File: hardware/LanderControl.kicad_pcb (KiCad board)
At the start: 4 copper layers, 140 x 54 mm, 161 parts, among them J2 Conn_01x04, J3 Conn_01x05, J5 MEM2051-00-195-00-A, Q1 BC846, Q2 BC846, Q3 BC846, Q4 BC846, Q5 BC846, Q6 BC846, Q7 BC846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

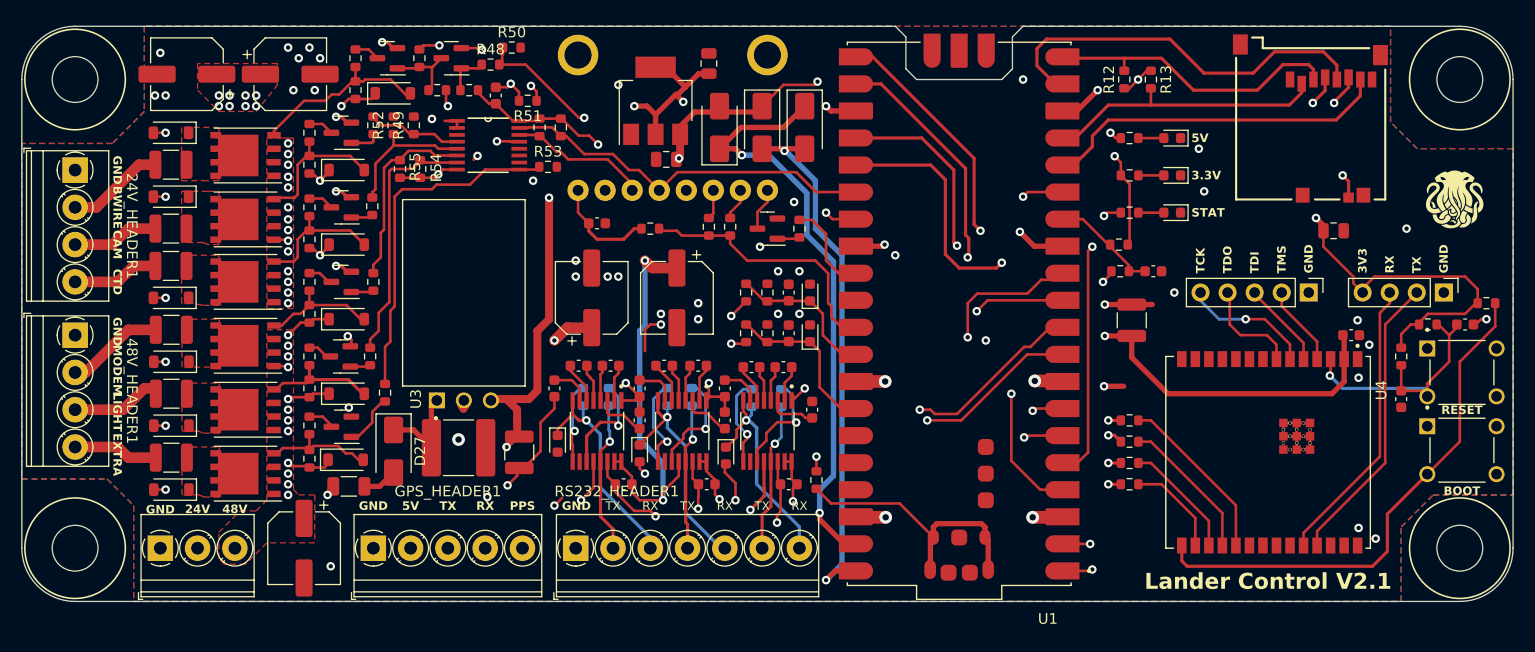
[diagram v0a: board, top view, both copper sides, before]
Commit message: Clean up tracks and vias, refill zones
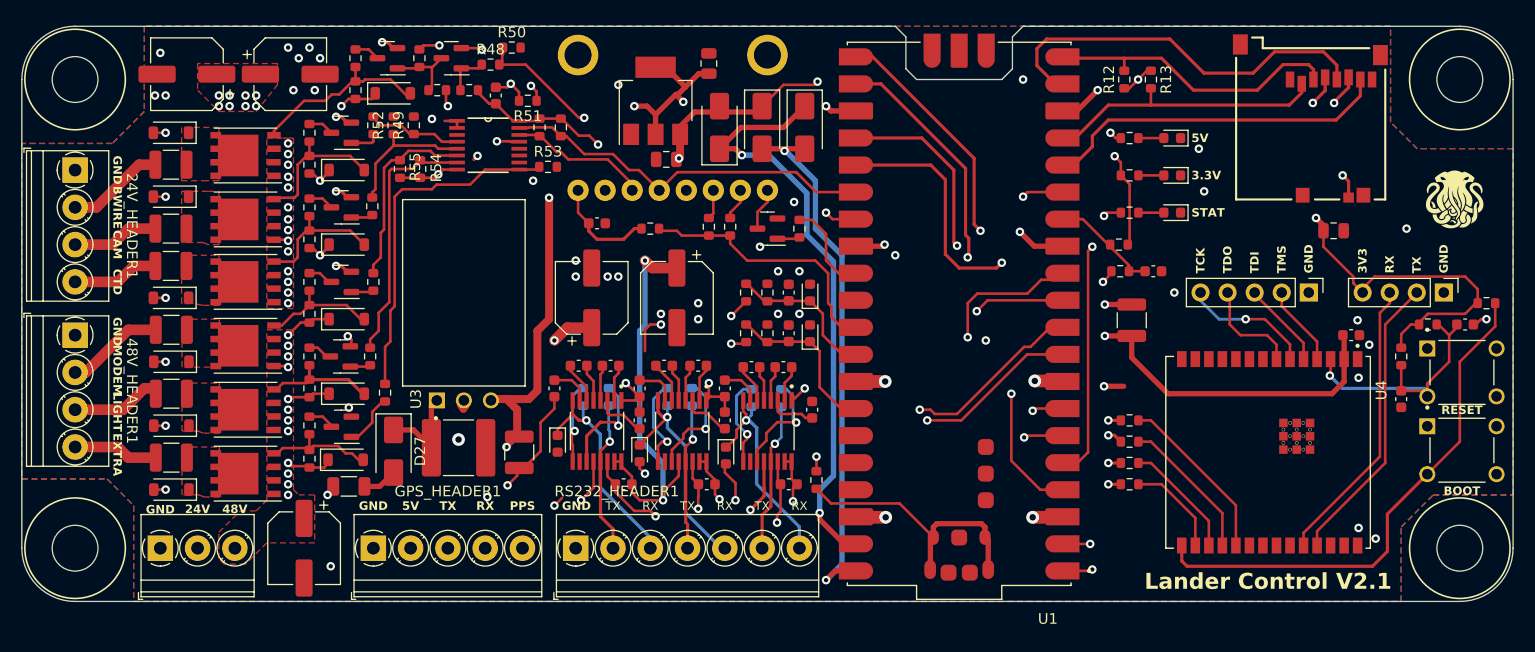
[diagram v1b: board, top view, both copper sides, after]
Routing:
- net GND: track 137.0 -> 119.8 mm
- net +3V3: track 317.5 -> 313.6 mm
- net GP12: track 34.1 -> 31.7 mm
- net GP28: track 15.6 -> 13.7 mm
- net GP27: track 14.3 -> 12.5 mm
- net GP26: track 25.0 -> 23.4 mm
- net +5V: track 105.6 -> 104.0 mm
- net GP3: track 27.3 -> 25.9 mm
- net +24V: track 91.3 -> 90.1 mm
- net GP13: track 26.6 -> 25.4 mm
- net GP21: track 36.0 -> 34.8 mm
- net Net-(D21-A): track 11.5 -> 10.3 mm
- net GP7: track 42.7 -> 41.6 mm
- net Net-(D26-K): track 56.1 -> 55.0 mm
- net /connectors/CTD_RX_232: track 21.4 -> 20.4 mm
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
